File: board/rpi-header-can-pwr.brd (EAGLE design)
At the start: 87 x 56.5 mm, 62 parts, among them IC1 MCP2515-E/SO, J1 U.FL, U3 BME280, U4 RFM69HCW, U5 INA219BIDCNT, X1 RJ45-8L21-S, X2 RASPI_BOARD_B+#_E3

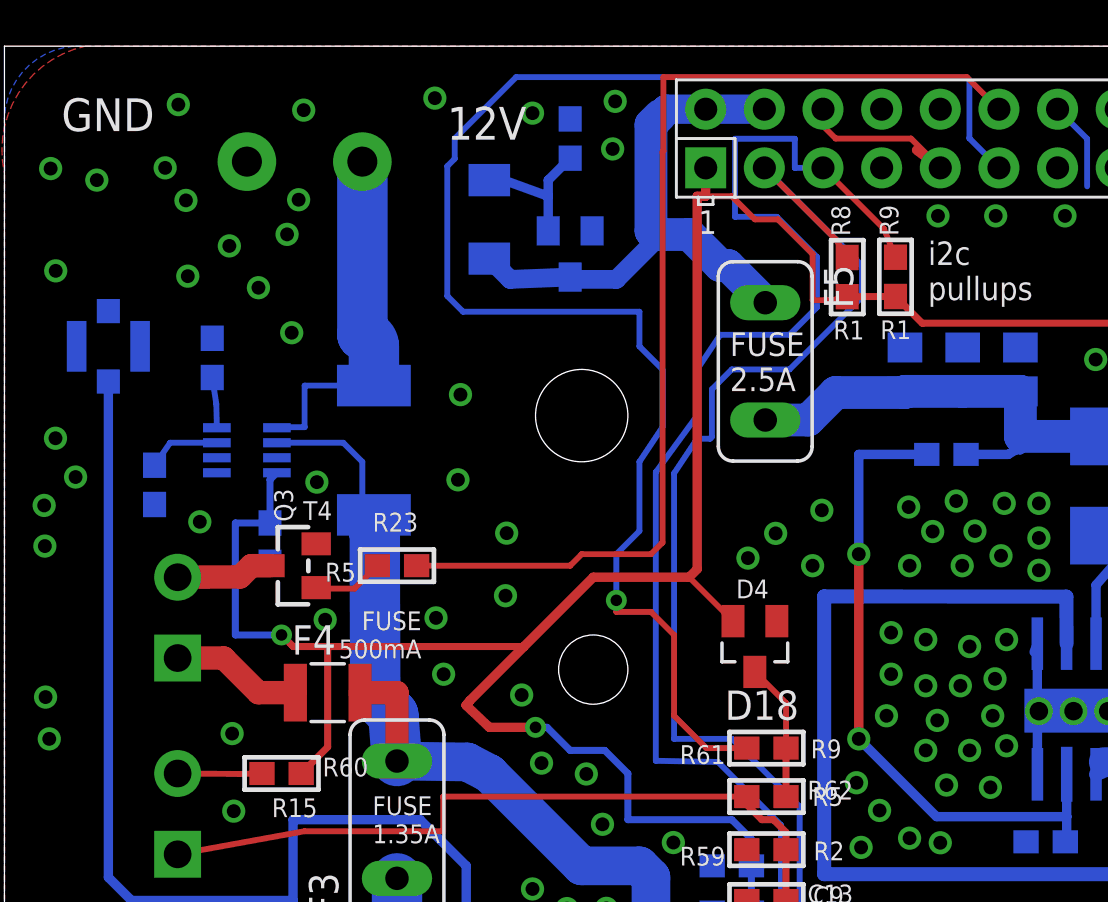
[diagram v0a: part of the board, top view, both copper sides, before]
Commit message: connect ina219 to i2c bus
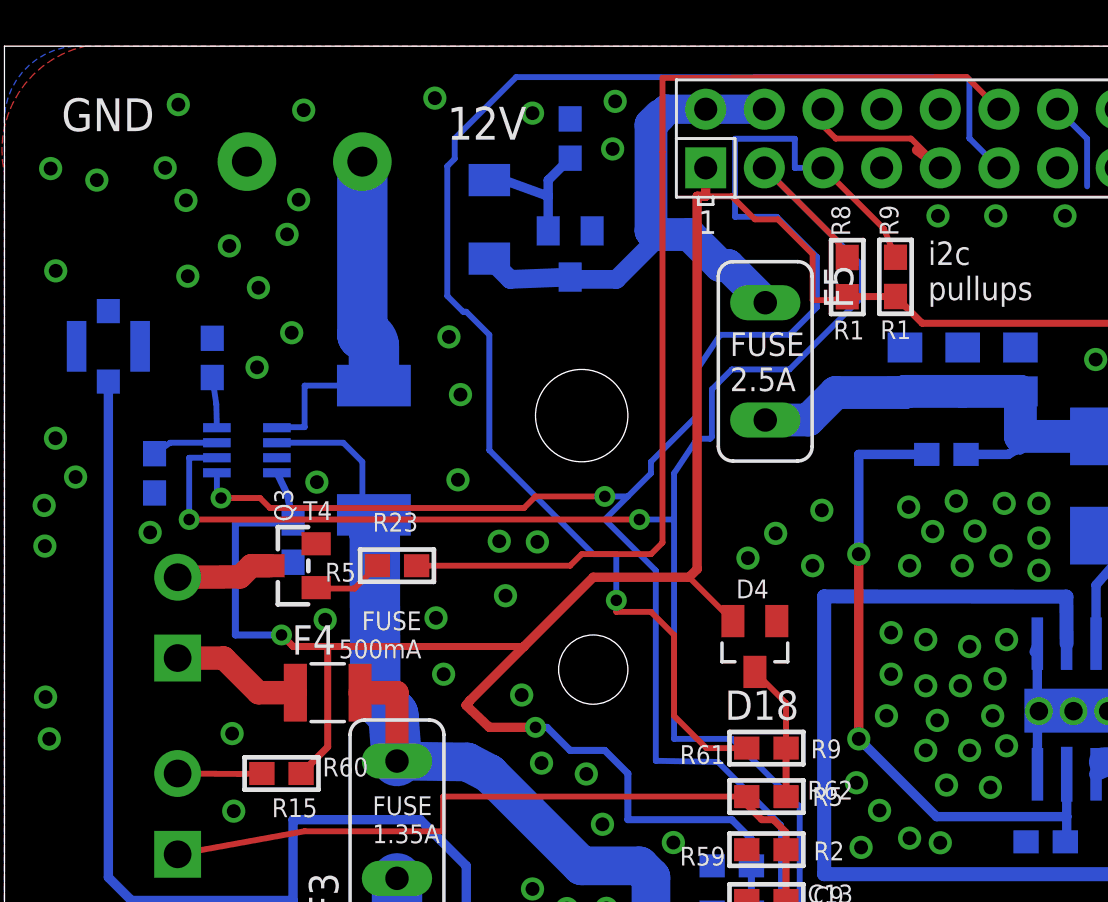
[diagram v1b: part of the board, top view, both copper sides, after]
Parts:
- moved C3 1.00 mm to (12.5, 35.0)
- moved R12 0.50 mm to (6.50, 38.0)
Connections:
- removed net SCL: U5.5
- removed net SDA: U5.6
- net I2C_SCL: now also U5.5
- net I2C_SDA: now also U5.6
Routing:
- net I2C_SDA: track 52.3 -> 77.1 mm, vias 0 -> 2
- net I2C_SCL: track 56.5 -> 77.7 mm, vias 0 -> 2
- net TAMPER: track 67.6 -> 62.3 mm
- net +3V3: track 250.1 -> 251.1 mm
- net GND: vias 239 -> 242
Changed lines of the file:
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@@
 <text x="71.68" y="30.23" size="0.8128" layer="121">C6</text>
 <text x="18.4" y="37.2" size="0.8128" layer="122" rot="MR90">0.1ohm</text>
-<text x="10.76" y="33.01" size="1.016" layer="122" rot="MR180">C1</text>
+<text x="11.71" y="32.89" size="1.016" layer="122" rot="MR180">C1</text>
 <text x="11.38" y="43.68" size="0.8128" layer="122" rot="MR0">R2</text>
-<text x="6.88" y="34.68" size="0.8128" layer="122" rot="MR0">R2</text>
+<text x="6.88" y="40.18" size="0.8128" layer="122" rot="MR0">R2</text>
 <text x="7.47" y="37.23" size="0.8128" layer="122" rot="MR90">INA219</text>
 </plain>
@@
 </element>
 <element name="U5" library="microbuilder" package="SOT23-8" value="INA219BIDCNT" x="10.5" y="39" rot="MR270"/>
-<element name="R12" library="microbuilder" package="0603" value="1K" x="6.5" y="37.5" rot="MR90"/>
+<element name="R12" library="microbuilder" package="0603" value="1K" x="6.5" y="38" rot="MR90"/>
 <element name="R13" library="microbuilder" package="0603" value="1K" x="9" y="43" rot="MR270"/>
 <element name="R19" library="microbuilder" package="2512" value="0.1/1% (PT2512FK-070R1L)" x="16" y="39" rot="MR90"/>
@@
 <element name="C22" library="microbuilder" package="0603" value="1u" x="55.5" y="42.5" rot="R90"/>
 <element name="C23" library="microbuilder" package="0603" value="1u" x="74.91" y="6.76" rot="R90"/>
-<element name="C3" library="microbuilder" package="0603" value="100n" x="11.5" y="35" rot="MR270"/>
+<element name="C3" library="microbuilder" package="0603" value="100n" x="12.5" y="35" rot="MR270"/>
 <element name="C4" library="microbuilder" package="0805" value="4,7u" x="51" y="26.5" rot="MR90"/>
 <element name="C6" library="microbuilder" package="0805" value="100n" x="53.45" y="26.53" rot="MR90"/>
@@
 <wire x1="59.3121" y1="43.35" x2="59.37" y2="43.4079" width="0.4064" layer="1"/>
 <contactref element="C3" pad="1"/>
-<wire x1="10" y1="35.85" x2="11.5" y2="35.85" width="0.3048" layer="16"/>
-<wire x1="11.5" y1="35.85" x2="11.5" y2="37.725" width="0.3048" layer="16"/>
-<wire x1="11.5" y1="37.725" x2="11.8" y2="38.025" width="0.3048" layer="16"/>
+<wire x1="10" y1="35.85" x2="12.5" y2="35.85" width="0.3048" layer="16"/>
+<wire x1="12.5" y1="35.85" x2="12.25" y2="37.095" width="0.3048" layer="16"/>
+<wire x1="12.25" y1="37.095" x2="11.8" y2="38.025" width="0.3048" layer="16"/>
 <contactref element="IC1" pad="18"/>
 <wire x1="60.1079" y1="43.37" x2="60.1079" y2="43.3043" width="0.3048" layer="1"/>
@@
 <via x="42.7" y="24.4" extent="1-16" drill="0.6"/>
 <via x="43.4" y="26.2" extent="1-16" drill="0.6"/>
-<via x="8.46" y="35.9" extent="1-16" drill="0.6"/>
+<via x="6.31" y="35.44" extent="1-16" drill="0.6"/>
 <via x="41.22" y="36.8" extent="1-16" drill="0.6"/>
 <via x="39.16" y="36.54" extent="1-16" drill="0.6"/>
@@
 <via x="19.64" y="37.72" extent="1-16" drill="0.6"/>
 <via x="19.75" y="41.41" extent="1-16" drill="0.6"/>
-<via x="21.75" y="35.41" extent="1-16" drill="0.6"/>
+<via x="21.43" y="35.06" extent="1-16" drill="0.6"/>
 <via x="19.02" y="29.3" extent="1-16" drill="0.6"/>
 <via x="1.78" y="28.31" extent="1-16" drill="0.6"/>
@@
 <contactref element="J4" pad="1"/>
 <contactref element="IC1" pad="9"/>
+<via x="23.08" y="35.03" extent="1-16" drill="0.6"/>
+<via x="19.25" y="43.91" extent="1-16" drill="0.6"/>
+<via x="10.94" y="42.59" extent="1-16" drill="0.6"/>
 </signal>
 <signal name="CAN_TX">
@@
 <wire x1="19.18" y1="51.305515625" x2="19.18" y2="45.68" width="0.254" layer="16"/>
 <wire x1="19.18" y1="45.68" x2="19.86" y2="45" width="0.254" layer="16"/>
-<wire x1="19.86" y1="45" x2="27.5" y2="45" width="0.254" layer="16"/>
-<wire x1="27.5" y1="45" x2="27.5" y2="43.5" width="0.254" layer="16"/>
-<wire x1="27.5" y1="38.5" x2="27.5" y2="35.5" width="0.254" layer="16"/>
-<wire x1="27.5" y1="35.5" x2="26.5" y2="34.5" width="0.254" layer="16"/>
+<wire x1="19.86" y1="45" x2="20" y2="45" width="0.254" layer="16"/>
 <wire x1="26.5" y1="34.5" x2="26.5" y2="32.5" width="0.254" layer="16"/>
 <via x="26.5" y="32.5" extent="1-16" drill="0.5"/>
@@
 <wire x1="29" y1="27.5" x2="30.4" y2="26.1" width="0.254" layer="1"/>
 <wire x1="30.4" y1="26.1" x2="32.15" y2="26.1" width="0.254" layer="1"/>
-<wire x1="27.5" y1="38.5" x2="28.5" y2="40" width="0.254" layer="16"/>
-<wire x1="28.5" y1="40" x2="28.5" y2="42.5" width="0.254" layer="16"/>
-<wire x1="28.5" y1="42.5" x2="27.5" y2="43.5" width="0.254" layer="16"/>
 <wire x1="19.18" y1="51.305515625" x2="19.5" y2="51.625515625" width="0.254" layer="16"/>
 <wire x1="19.5" y1="51.625515625" x2="19.5" y2="52.5" width="0.254" layer="16"/>
+<wire x1="26.5" y1="34.5" x2="25.5" y2="34.5" width="0.254" layer="16"/>
+<wire x1="25.5" y1="34.5" x2="21" y2="39" width="0.254" layer="16"/>
+<wire x1="20" y1="45" x2="21" y2="44" width="0.254" layer="16"/>
+<wire x1="21" y1="44" x2="21" y2="39" width="0.254" layer="16"/>
 </signal>
 <signal name="SCK">
@@
 <wire x1="35" y1="18" x2="34.44" y2="18" width="0.254" layer="16"/>
 <wire x1="34.44" y1="18" x2="34.44" y2="23.57" width="0.254" layer="16"/>
-<wire x1="29" y1="26.5" x2="29" y2="38" width="0.254" layer="16"/>
+<wire x1="29" y1="26.5" x2="29" y2="36" width="0.254" layer="16"/>
+<wire x1="29" y1="36" x2="29" y2="38" width="0.254" layer="16"/>
 <wire x1="29" y1="38" x2="30" y2="39.5" width="0.254" layer="16"/>
 <wire x1="30" y1="39.5" x2="30.56" y2="39.5" width="0.254" layer="16"/>
@@
 <wire x1="30.64" y1="41.64" x2="30.64" y2="39.58" width="0.254" layer="16"/>
 <wire x1="30.64" y1="39.58" x2="30.56" y2="39.5" width="0.254" layer="16"/>
+<contactref element="U5" pad="6"/>
+<wire x1="29" y1="36" x2="27.5" y2="36" width="0.254" layer="16"/>
+<via x="27.5" y="36" extent="1-16" drill="0.5"/>
+<wire x1="9.2" y1="38.675" x2="8" y2="38.675" width="0.254" layer="16"/>
+<wire x1="8" y1="38.675" x2="8" y2="36" width="0.254" layer="16"/>
+<via x="8" y="36" extent="1-16" drill="0.5"/>
+<wire x1="8" y1="36" x2="27.5" y2="36" width="0.254" layer="1"/>
 </signal>
 <signal name="I2C_SCL">
@@
 <wire x1="33.63" y1="22.77" x2="30.9" y2="25.5" width="0.254" layer="16"/>
 <wire x1="30.9" y1="25.5" x2="28.21" y2="25.55" width="0.254" layer="16"/>
-<wire x1="28.21" y1="25.55" x2="28.21" y2="38.05" width="0.254" layer="16"/>
+<wire x1="28.21" y1="25.55" x2="28.21" y2="33.79" width="0.254" layer="16"/>
 <wire x1="30" y1="42.5" x2="30" y2="40.5" width="0.254" layer="16"/>
-<wire x1="30" y1="40.5" x2="28.21" y2="38.05" width="0.254" layer="16"/>
 <wire x1="35.45" y1="51.23" x2="34.23" y2="51.23" width="0.254" layer="16"/>
 <wire x1="34.23" y1="51.23" x2="34.23" y2="52.49" width="0.254" layer="16"/>
@@
 <wire x1="38.59" y1="47.36" x2="38.09" y2="48.59" width="0.254" layer="1"/>
 <wire x1="38.09" y1="48.59" x2="35.45" y2="51.23" width="0.254" layer="1"/>
+<contactref element="U5" pad="5"/>
+<wire x1="28.21" y1="33.79" x2="26" y2="36" width="0.254" layer="16"/>
+<wire x1="26" y1="36" x2="27" y2="37" width="0.254" layer="16"/>
+<wire x1="27" y1="37" x2="28" y2="38" width="0.254" layer="16"/>
+<wire x1="28" y1="38" x2="28" y2="38.5" width="0.254" layer="16"/>
+<wire x1="28" y1="38.5" x2="30" y2="40.5" width="0.254" layer="16"/>
+<wire x1="9.2" y1="38.025" x2="9.2" y2="37.11" width="0.254" layer="16"/>
+<wire x1="9.2" y1="37.11" x2="9.38" y2="36.93" width="0.254" layer="16"/>
+<via x="9.38" y="36.93" extent="1-16" drill="0.5"/>
+<wire x1="9.38" y1="36.93" x2="11.07" y2="36.93" width="0.254" layer="1"/>
+<wire x1="11.07" y1="36.93" x2="11.5" y2="36.5" width="0.254" layer="1"/>
+<wire x1="27" y1="37" x2="26" y2="37" width="0.254" layer="16"/>
+<via x="26" y="37" extent="1-16" drill="0.5"/>
+<wire x1="26" y1="37" x2="23" y2="37" width="0.254" layer="1"/>
+<wire x1="23" y1="37" x2="22.5" y2="36.5" width="0.254" layer="1"/>
+<wire x1="22.5" y1="36.5" x2="11.5" y2="36.5" width="0.254" layer="1"/>
 </signal>
 <signal name="CAN_PWR">
@@
 <contactref element="X2" pad="12"/>
 <wire x1="43.07" y1="53.77" x2="41.68" y2="55.16" width="0.254" layer="1"/>
-<wire x1="41.68" y1="55.16" x2="28.5390125" y2="55.16" width="0.254" layer="1"/>
-<wire x1="28.5390125" y1="55.16" x2="28.5390125" y2="51.9590125" width="0.254" layer="1"/>
-<wire x1="28.5390125" y1="51.9590125" x2="28.5" y2="51.92" width="0.254" layer="1"/>
+<wire x1="41.68" y1="55.16" x2="28.4990125" y2="55.13" width="0.254" layer="1"/>
+<wire x1="28.4990125" y1="55.13" x2="28.4990125" y2="51.9490125" width="0.254" layer="1"/>
+<wire x1="28.4990125" y1="51.9490125" x2="28.5" y2="51.92" width="0.254" layer="1"/>
 <wire x1="28.5" y1="51.92" x2="28.5" y2="35" width="0.254" layer="1"/>
 <wire x1="28.5" y1="35" x2="28" y2="34.5" width="0.254" layer="1"/>
@@
 <contactref element="R12" pad="2"/>
 <wire x1="9.2" y1="39.325" x2="7.175" y2="39.325" width="0.254" layer="16"/>
-<wire x1="7.175" y1="39.325" x2="6.5" y2="38.35" width="0.254" layer="16"/>
-</signal>
-<signal name="SDA">
-<contactref element="U5" pad="6"/>
-</signal>
-<signal name="SCL">
-<contactref element="U5" pad="5"/>
+<wire x1="7.175" y1="39.325" x2="6.5" y2="38.85" width="0.254" layer="16"/>
 </signal>
 <signal name="PRE_SENSE_12V">
